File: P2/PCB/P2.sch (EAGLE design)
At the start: 28 parts, among them CON1 Volume, CON2 Noritake, IC1 ATMEGA48/88/168-AU, IC2 TPIC6B595DW, IC3 TPIC6B595DW, K1 G6H2-100, Q1 16MHz

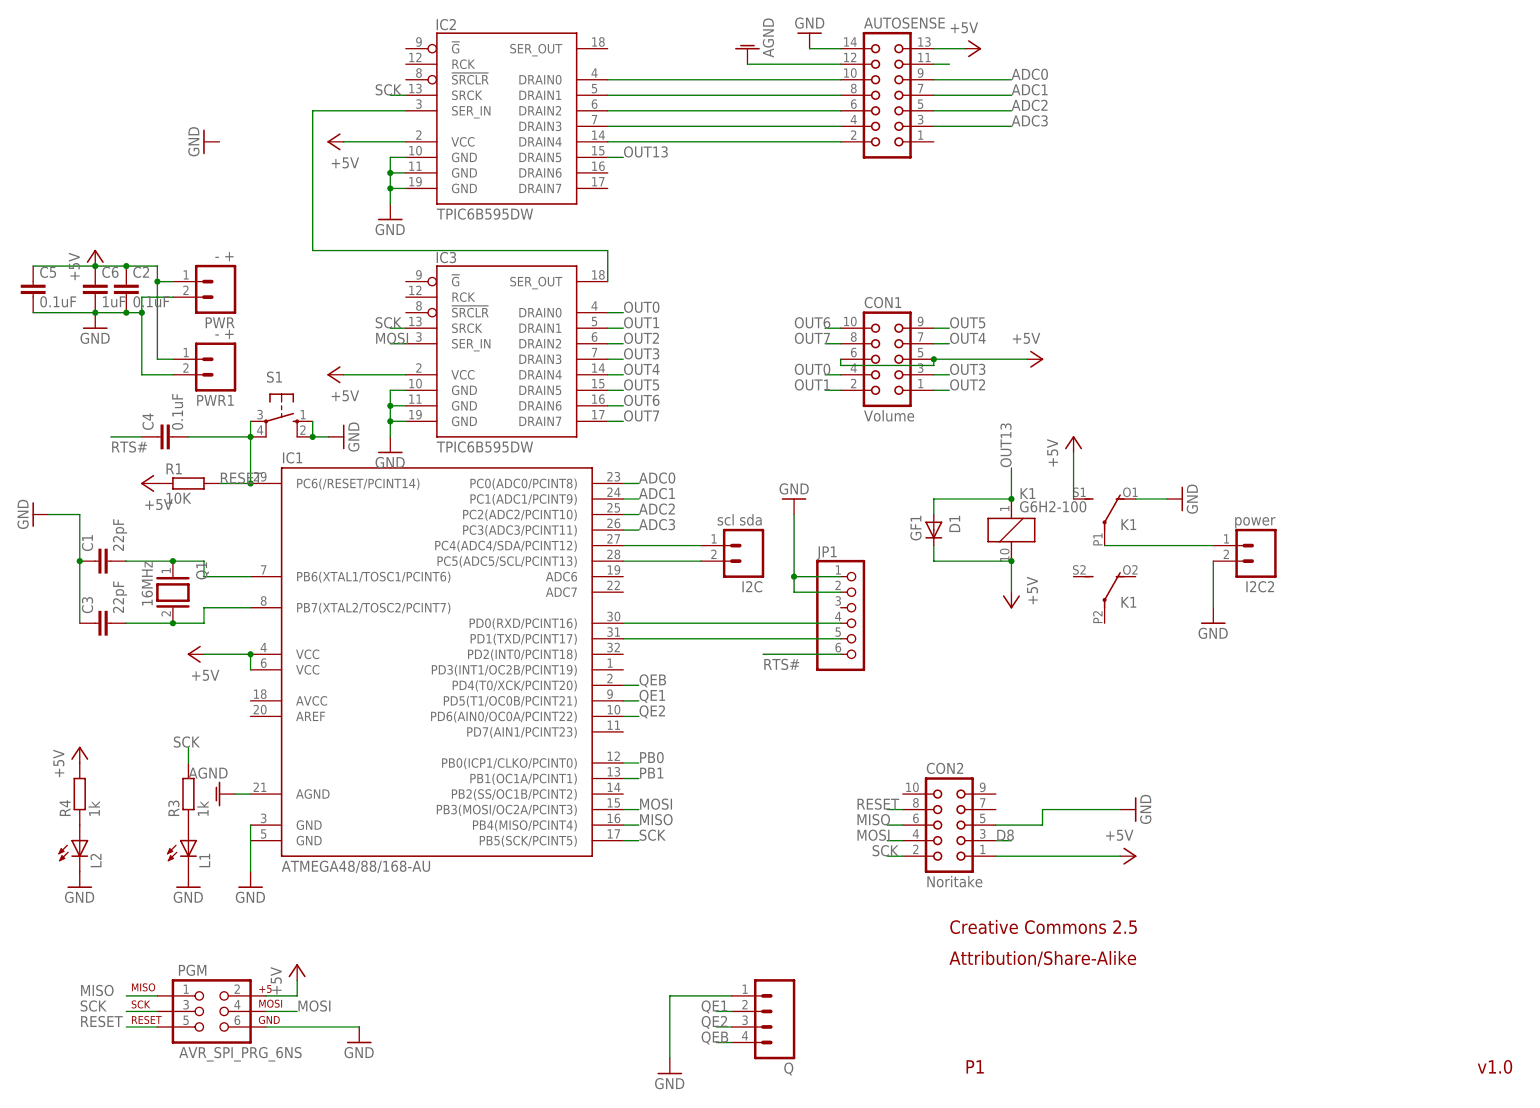
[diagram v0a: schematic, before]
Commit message: Added AutoSense, missing connections on P2
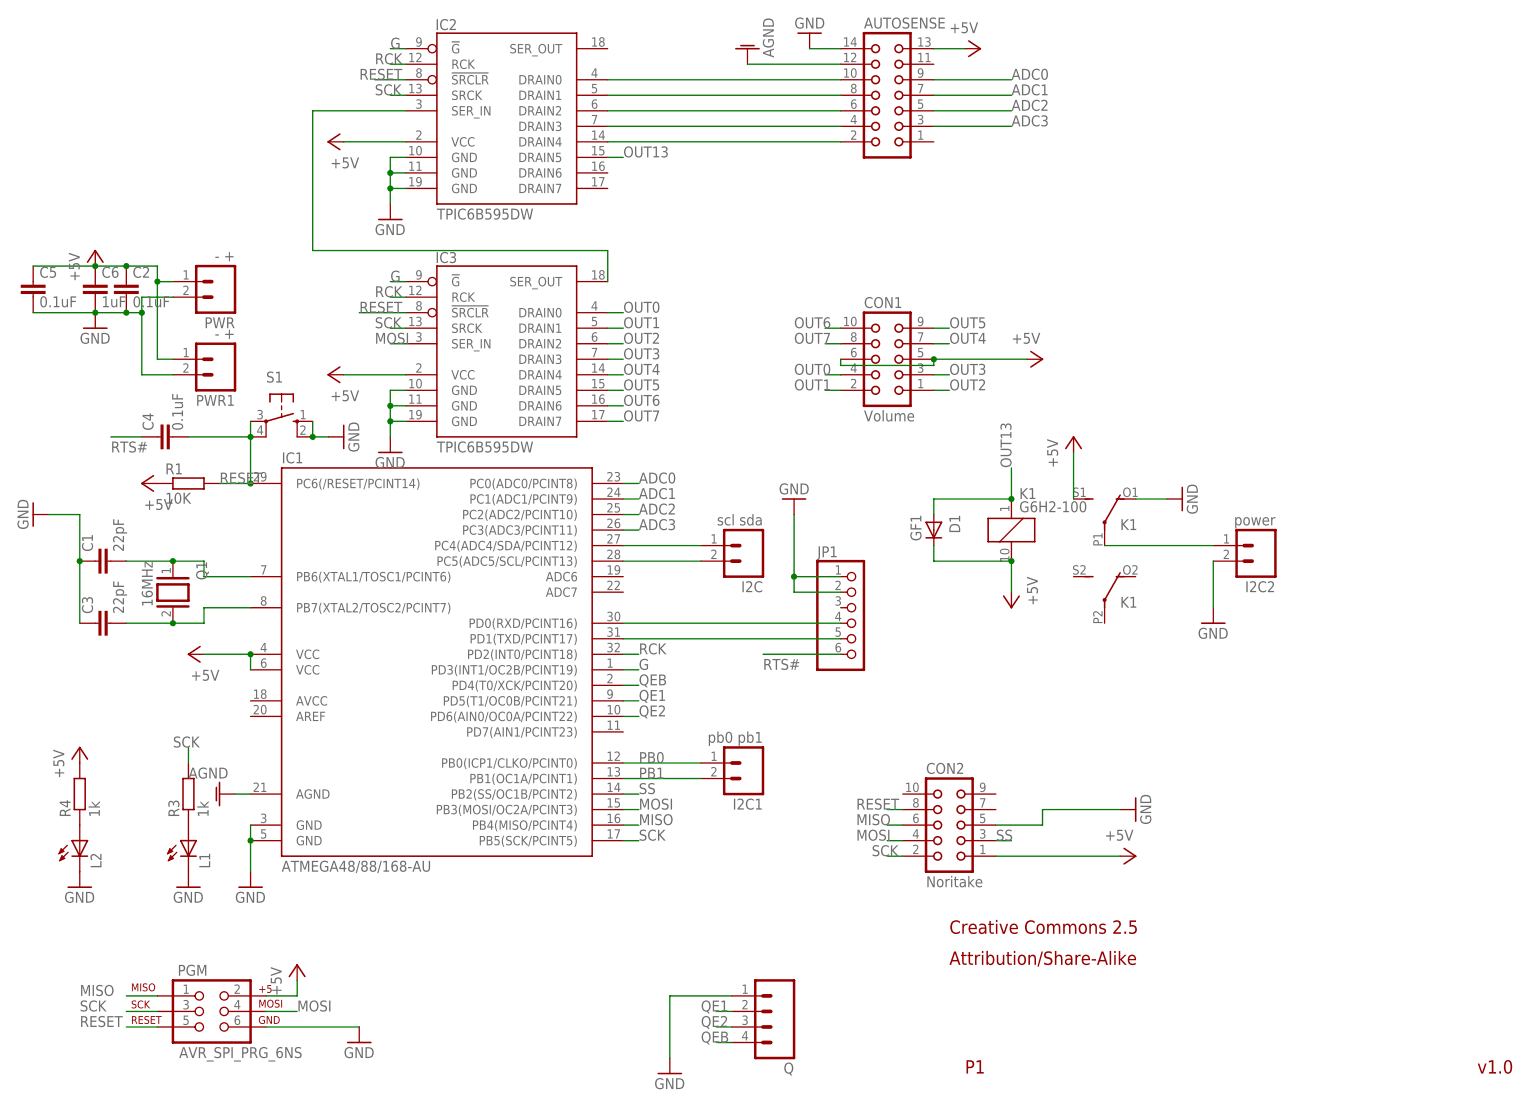
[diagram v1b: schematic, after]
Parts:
- added I2C1: pb0 pb1, SparkFun:M02PTH
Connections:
- removed net D8: CON2.3
- removed net N$14: AUTOSENSE.11
- new net G: IC1.PD3(INT1/OC2B/PCINT19), IC2.!G, IC3.!G
- new net RCK: IC1.PD2(INT0/PCINT18), IC2.RCK, IC3.RCK
- new net SS: CON2.3, IC1.PB2(SS/OC1B/PCINT2)
- net GND: now also IC1.GND@2
- net PB0: now also I2C1.1
- net PB1: now also I2C1.2
- net RESET: now also IC2.!SRCLR, IC3.!SRCLR
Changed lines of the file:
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@@
 <part name="CON1" library="con-harting-lars" deviceset="CON10L" device="" value="Volume"/>
 <part name="Q1" library="special" deviceset="XTAL/S" device="" value="16MHz"/>
-<part name="GND3" library="supply1" deviceset="GND" device=""/>
 <part name="CON2" library="con-harting-lars" deviceset="CON10L" device="" value="Noritake"/>
 <part name="I2C" library="SparkFun" deviceset="M02" device="PTH" value="scl sda"/>
@@
 <part name="GND15" library="supply1" deviceset="GND" device=""/>
 <part name="GND16" library="supply1" deviceset="GND" device=""/>
+<part name="I2C1" library="SparkFun" deviceset="M02" device="PTH" value="pb0 pb1"/>
 </parts>
 <sheets>
@@
 <instance part="CON1" gate="G$1" x="142.24" y="124.46"/>
 <instance part="Q1" gate="G$1" x="25.4" y="86.36" rot="R270"/>
-<instance part="GND3" gate="1" x="30.48" y="160.02" rot="R270"/>
 <instance part="CON2" gate="G$1" x="152.4" y="48.26"/>
 <instance part="I2C" gate="G$1" x="119.38" y="93.98" rot="R180"/>
@@
 <instance part="GND15" gate="1" x="195.58" y="81.28"/>
 <instance part="GND16" gate="1" x="190.5" y="101.6" rot="R90"/>
+<instance part="I2C1" gate="G$1" x="119.38" y="58.42" rot="R180"/>
 </instances>
 <busses>
@@
 <pinref part="IC1" gate="1" pin="GND@1"/>
 <pinref part="GND1" gate="1" pin="GND"/>
-<wire x1="38.1" y1="48.26" x2="38.1" y2="40.64" width="0.1524" layer="91"/>
+<wire x1="38.1" y1="48.26" x2="38.1" y2="45.72" width="0.1524" layer="91"/>
+<pinref part="IC1" gate="1" pin="GND@2"/>
+<junction x="38.1" y="45.72"/>
+<wire x1="38.1" y1="45.72" x2="38.1" y2="40.64" width="0.1524" layer="91"/>
 </segment>
 <segment>
@@
 </segment>
 </net>
-<net name="D8" class="0">
+<net name="SS" class="0">
 <segment>
 <wire x1="160.02" y1="45.72" x2="162.56" y2="45.72" width="0.1524" layer="91"/>
 <label x="160.02" y="45.72" size="1.778" layer="95"/>
 <pinref part="CON2" gate="G$1" pin="3"/>
+</segment>
+<segment>
+<pinref part="IC1" gate="1" pin="PB2(SS/OC1B/PCINT2)"/>
+<wire x1="99.06" y1="53.34" x2="101.6" y2="53.34" width="0.1524" layer="91"/>
+<label x="101.6" y="53.34" size="1.778" layer="95"/>
 </segment>
 </net>
@@
 <pinref part="PGM" gate="G$1" pin="5"/>
 </segment>
+<segment>
+<pinref part="IC2" gate="G$1" pin="!SRCLR"/>
+<wire x1="63.5" y1="170.18" x2="58.42" y2="170.18" width="0.1524" layer="91"/>
+<label x="55.88" y="170.18" size="1.778" layer="95"/>
+</segment>
+<segment>
+<pinref part="IC3" gate="G$1" pin="!SRCLR"/>
+<wire x1="63.5" y1="132.08" x2="55.88" y2="132.08" width="0.1524" layer="91"/>
+<label x="55.88" y="132.08" size="1.778" layer="95"/>
+</segment>
 </net>
 <net name="QE1" class="0">
@@
 </segment>
 </net>
-<net name="N$8" class="0">
-<segment>
-<pinref part="IC1" gate="1" pin="PC5(ADC5/SCL/PCINT13)"/>
-<pinref part="I2C" gate="G$1" pin="2"/>
-<wire x1="99.06" y1="91.44" x2="111.76" y2="91.44" width="0.1524" layer="91"/>
-</segment>
-</net>
 <net name="OUT0" class="0">
 <segment>
@@
 <segment>
 <pinref part="IC1" gate="1" pin="PB1(OC1A/PCINT1)"/>
-<wire x1="99.06" y1="55.88" x2="101.6" y2="55.88" width="0.1524" layer="91"/>
 <label x="101.6" y="55.88" size="1.778" layer="95"/>
+<pinref part="I2C1" gate="G$1" pin="2"/>
+<wire x1="99.06" y1="55.88" x2="111.76" y2="55.88" width="0.1524" layer="91"/>
 </segment>
 </net>
@@
 <segment>
 <pinref part="IC1" gate="1" pin="PB0(ICP1/CLKO/PCINT0)"/>
-<wire x1="99.06" y1="58.42" x2="101.6" y2="58.42" width="0.1524" layer="91"/>
 <label x="101.6" y="58.42" size="1.778" layer="95"/>
+<pinref part="I2C1" gate="G$1" pin="1"/>
+<wire x1="99.06" y1="58.42" x2="111.76" y2="58.42" width="0.1524" layer="91"/>
 </segment>
 </net>
@@
 <wire x1="149.86" y1="162.56" x2="162.56" y2="162.56" width="0.1524" layer="91"/>
 <label x="162.56" y="162.56" size="1.778" layer="95"/>
-</segment>
-</net>
-<net name="N$14" class="0">
-<segment>
-<pinref part="AUTOSENSE" gate="G$1" pin="11"/>
-<wire x1="152.4" y1="172.72" x2="149.86" y2="172.72" width="0.1524" layer="91"/>
 </segment>
 </net>
@@
 </segment>
 </net>
+<net name="G" class="0">
+<segment>
+<pinref part="IC2" gate="G$1" pin="!G"/>
+<wire x1="63.5" y1="175.26" x2="60.96" y2="175.26" width="0.1524" layer="91"/>
+<label x="60.96" y="175.26" size="1.778" layer="95"/>
+</segment>
+<segment>
+<pinref part="IC3" gate="G$1" pin="!G"/>
+<wire x1="63.5" y1="137.16" x2="60.96" y2="137.16" width="0.1524" layer="91"/>
+<label x="60.96" y="137.16" size="1.778" layer="95"/>
+</segment>
+<segment>
+<pinref part="IC1" gate="1" pin="PD3(INT1/OC2B/PCINT19)"/>
+<wire x1="99.06" y1="73.66" x2="101.6" y2="73.66" width="0.1524" layer="91"/>
+<label x="101.6" y="73.66" size="1.778" layer="95"/>
+</segment>
+</net>
+<net name="RCK" class="0">
+<segment>
+<pinref part="IC2" gate="G$1" pin="RCK"/>
+<wire x1="63.5" y1="172.72" x2="60.96" y2="172.72" width="0.1524" layer="91"/>
+<label x="58.42" y="172.72" size="1.778" layer="95"/>
+</segment>
+<segment>
+<pinref part="IC3" gate="G$1" pin="RCK"/>
+<wire x1="63.5" y1="134.62" x2="60.96" y2="134.62" width="0.1524" layer="91"/>
+<label x="58.42" y="134.62" size="1.778" layer="95"/>
+</segment>
+<segment>
+<pinref part="IC1" gate="1" pin="PD2(INT0/PCINT18)"/>
+<wire x1="99.06" y1="76.2" x2="101.6" y2="76.2" width="0.1524" layer="91"/>
+<label x="101.6" y="76.2" size="1.778" layer="95"/>
+</segment>
+</net>
+<net name="N$8" class="0">
+<segment>
+<pinref part="IC1" gate="1" pin="PC5(ADC5/SCL/PCINT13)"/>
+<pinref part="I2C" gate="G$1" pin="2"/>
+<wire x1="99.06" y1="91.44" x2="111.76" y2="91.44" width="0.1524" layer="91"/>
+</segment>
+</net>
 </nets>
 </sheet>
 </sheets>
+<errors>
+</errors>
 </schematic>
 </drawing>

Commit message: Jumper for IR and SS, silkscreen cleanups.
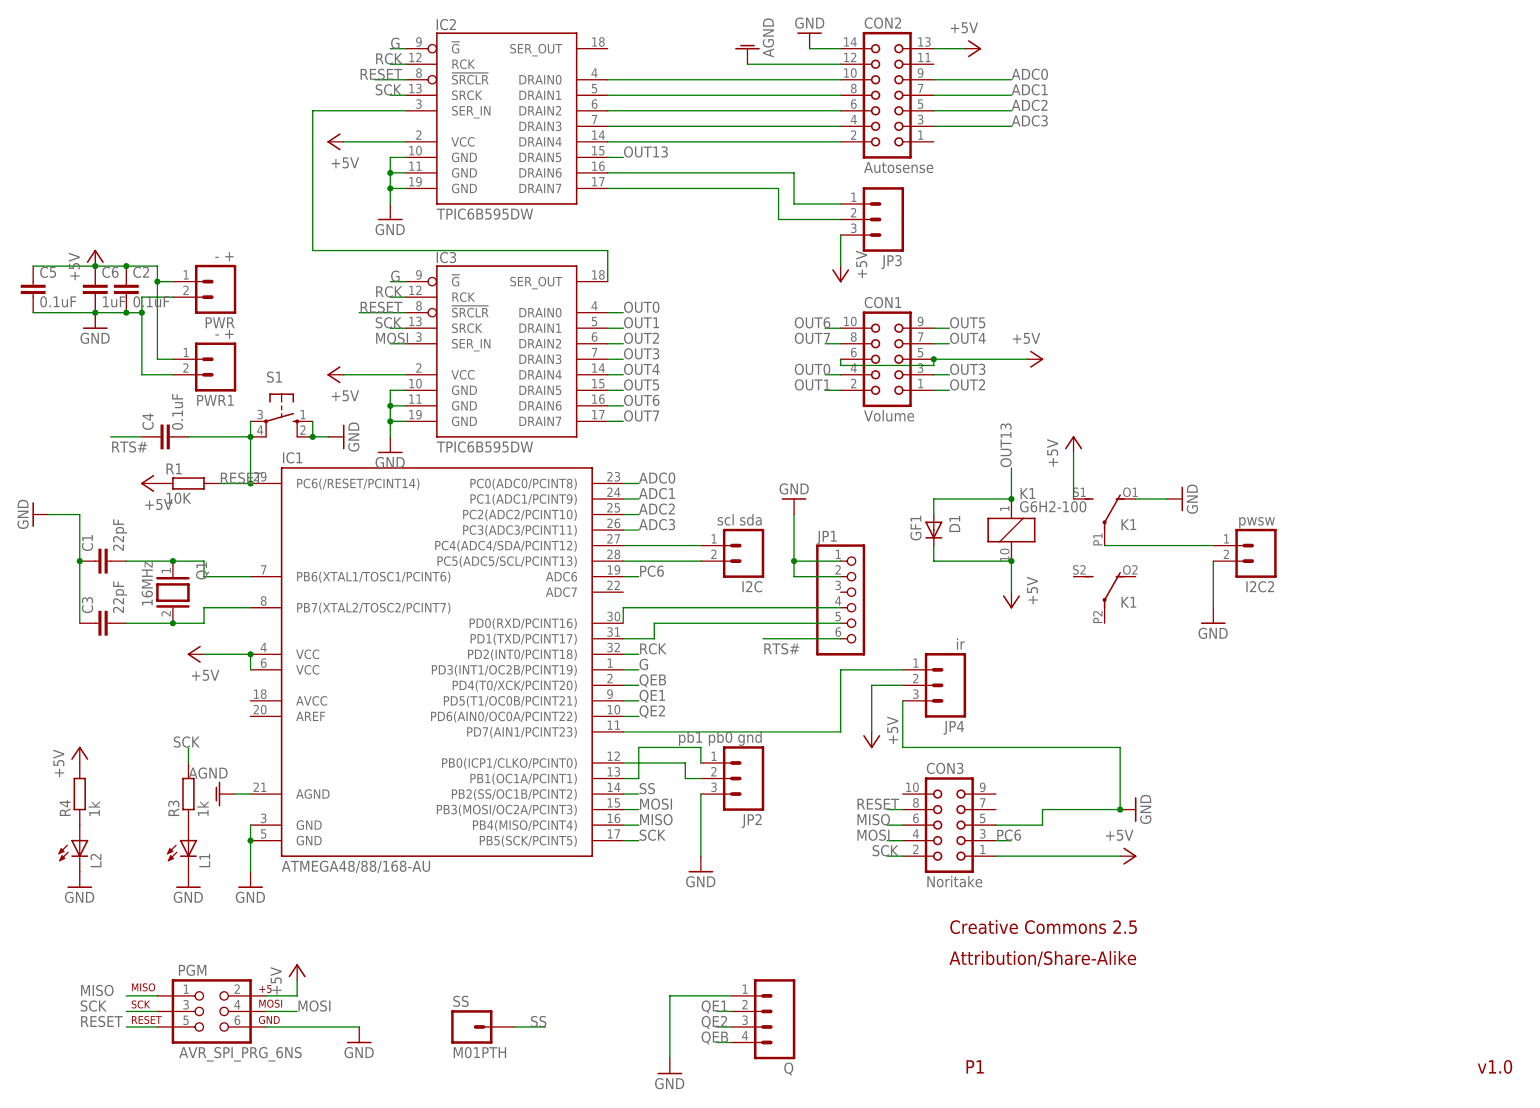
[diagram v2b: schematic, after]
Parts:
- removed AUTOSENSE: (no value), con-harting-lars:CON14L
- removed I2C1: pb0 pb1, SparkFun:M02PTH
- added CON3: Noritake, con-harting-lars:CON10L
- added JP2: pb1 pb0 gnd, SparkFun-Connectors:M03PTH
- added JP3: (no value), SparkFun-Connectors:M03PTH
- added JP4: ir, SparkFun-Connectors:M03PTH
- added SS: M01PTH, SparkFun-Connectors:M01PTH
- CON2: value Noritake -> Autosense; device con-harting-lars:CON10L -> con-harting-lars:CON14L
- I2C2: value power -> pwsw
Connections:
- removed net PB0: I2C1.1, IC1.PB0(ICP1/CLKO/PCINT0)
- removed net PB1: I2C1.2, IC1.PB1(OC1A/PCINT1)
- new net N$10: IC1.PB0(ICP1/CLKO/PCINT0), JP2.2
- new net N$11: IC2.DRAIN6, JP3.1
- new net N$12: IC2.DRAIN7, JP3.2
- new net N$14: IC1.PD7(AIN1/PCINT23), JP4.1
- new net N$9: IC1.PB1(OC1A/PCINT1), JP2.1
- new net PC6: CON3.3, IC1.ADC6
- net +5V: now also CON2.13, CON3.1, JP3.3, JP4.2; no longer AUTOSENSE.13, CON2.1
- net ADC0: now also CON2.9; no longer AUTOSENSE.9
- net ADC1: now also CON2.7; no longer AUTOSENSE.7
- net ADC2: now also CON2.5; no longer AUTOSENSE.5
- net ADC3: now also CON2.3; no longer AUTOSENSE.3
- net AGND: now also CON2.12; no longer AUTOSENSE.12
- net GND: now also CON2.14, CON3.5, JP2.3, JP4.3; no longer AUTOSENSE.14, CON2.5
- net MISO: now also CON3.6; no longer CON2.6
- net MOSI: now also CON3.4; no longer CON2.4
- net OUT10: now also CON2.6; no longer AUTOSENSE.6
- net OUT11: now also CON2.4; no longer AUTOSENSE.4
- net OUT12: now also CON2.2; no longer AUTOSENSE.2
- net OUT8: now also CON2.10; no longer AUTOSENSE.10
- net OUT9: now also CON2.8; no longer AUTOSENSE.8
- net RESET: now also CON3.8; no longer CON2.8
- net SCK: now also CON3.2; no longer CON2.2
- net SS: now also SS.1; no longer CON2.3
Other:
- moved on the sheet: JP1

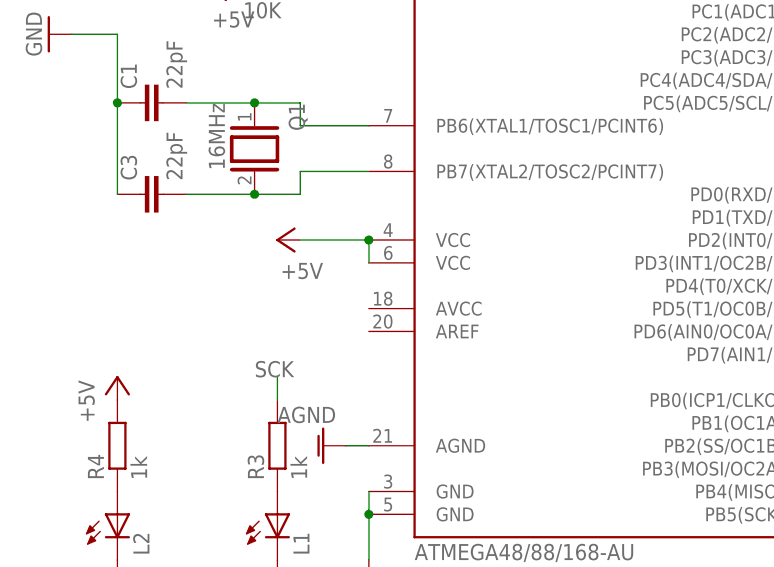
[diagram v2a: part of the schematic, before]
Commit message: Connect AVCC
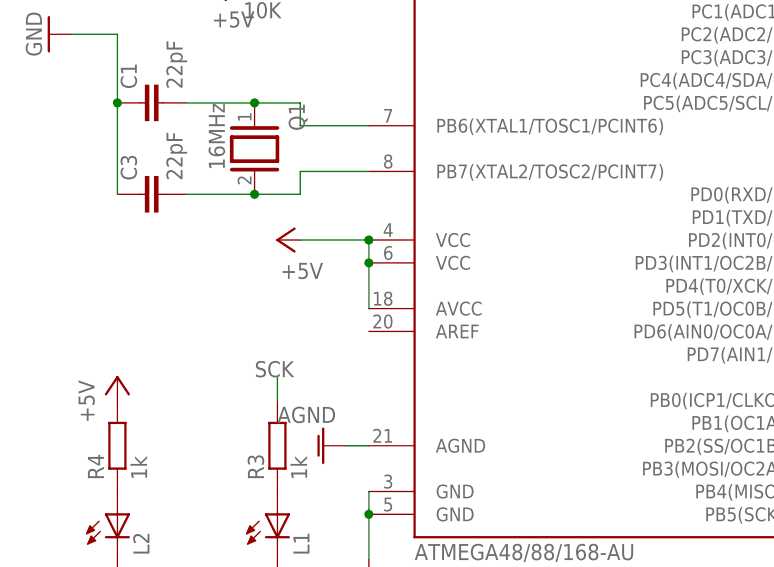
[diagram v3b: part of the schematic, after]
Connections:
- net +5V: now also IC1.AVCC
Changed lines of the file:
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@@
 <wire x1="38.1" y1="76.2" x2="38.1" y2="73.66" width="0.1524" layer="91"/>
 <junction x="38.1" y="76.2"/>
+<pinref part="IC1" gate="1" pin="AVCC"/>
+<wire x1="38.1" y1="68.58" x2="38.1" y2="73.66" width="0.1524" layer="91"/>
+<junction x="38.1" y="73.66"/>
 </segment>
 <segment>
